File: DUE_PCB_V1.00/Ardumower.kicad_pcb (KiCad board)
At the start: 2 copper layers, 169.9 x 97 mm, 81 parts, among them J1 9V IN, J10 Sonar_R, J11 Sonar_C, J12 Sonar_L, J13 P_Right, J14 Buzzer, J15 Button, J16 US1, J17 US2, J18 US3, J19 P_Left, J2 I2C0_1, J20 Remote, J21 PCB_2, J22 Ser0, J23 Ser1, J24 Ser2, J25 5V IN, J26 Cutter1, J27 MotorR, J28 MotorL, J29 3.3V IN, J3 I2C0_2, J30 I2C1_2, J31 Ser3, J32 24V In, J33 ReserveD8, J34 ReserveD9, J35 ReserveD49, J36 ReserveA10, J37 RPM_Mow, J38 ODO_Left, J39 ODO_Right, J4 I2C1_1, J5 Bumper, J6 Drop_Left, J7 Drop_Right, J8 Tilt, J9 Rain, U1 MC33926, U2 MC33926

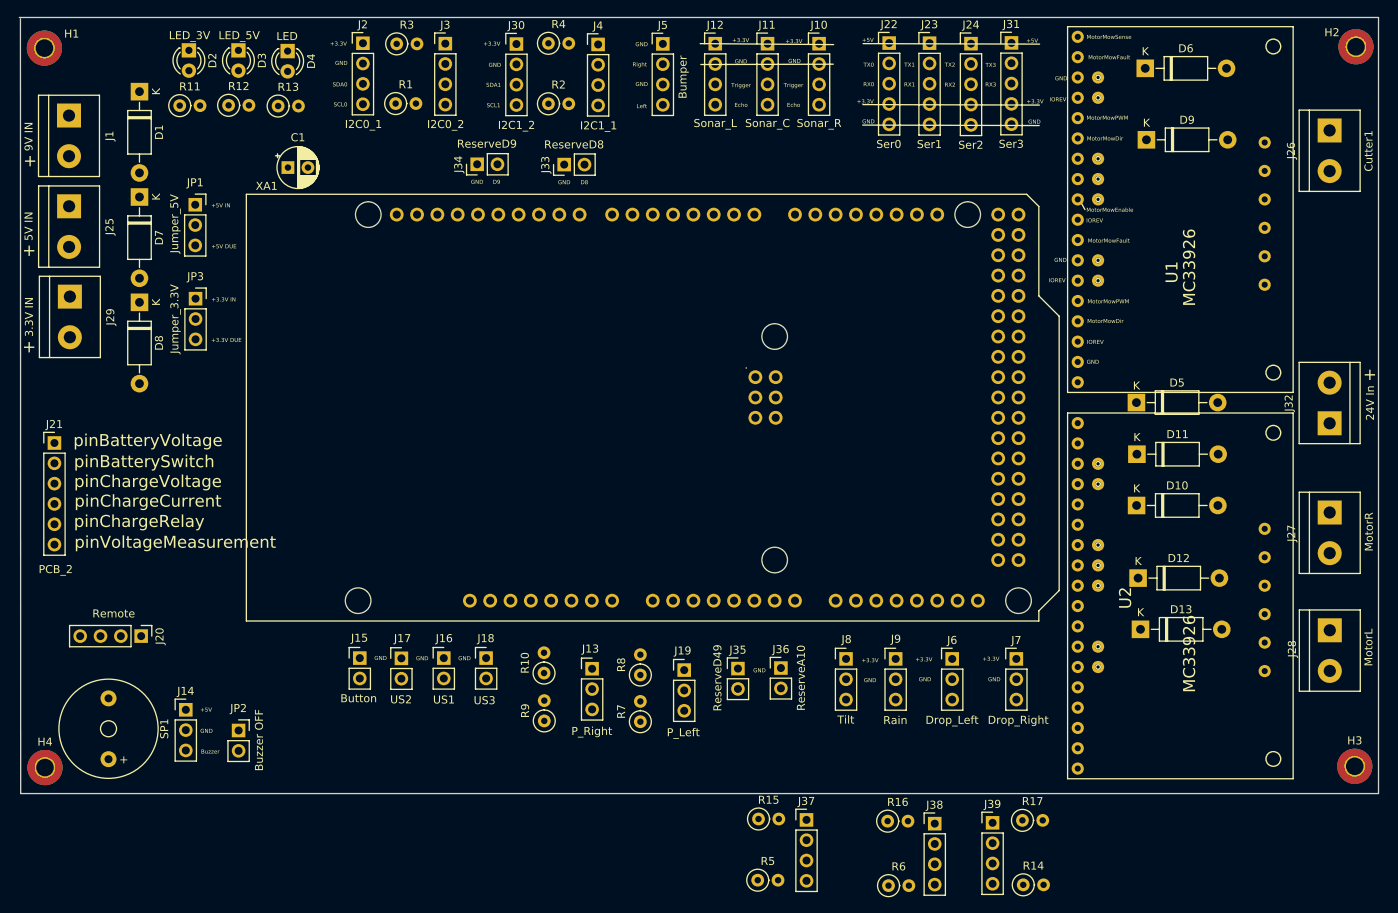
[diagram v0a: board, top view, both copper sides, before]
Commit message: Sorting Connectors on PCB
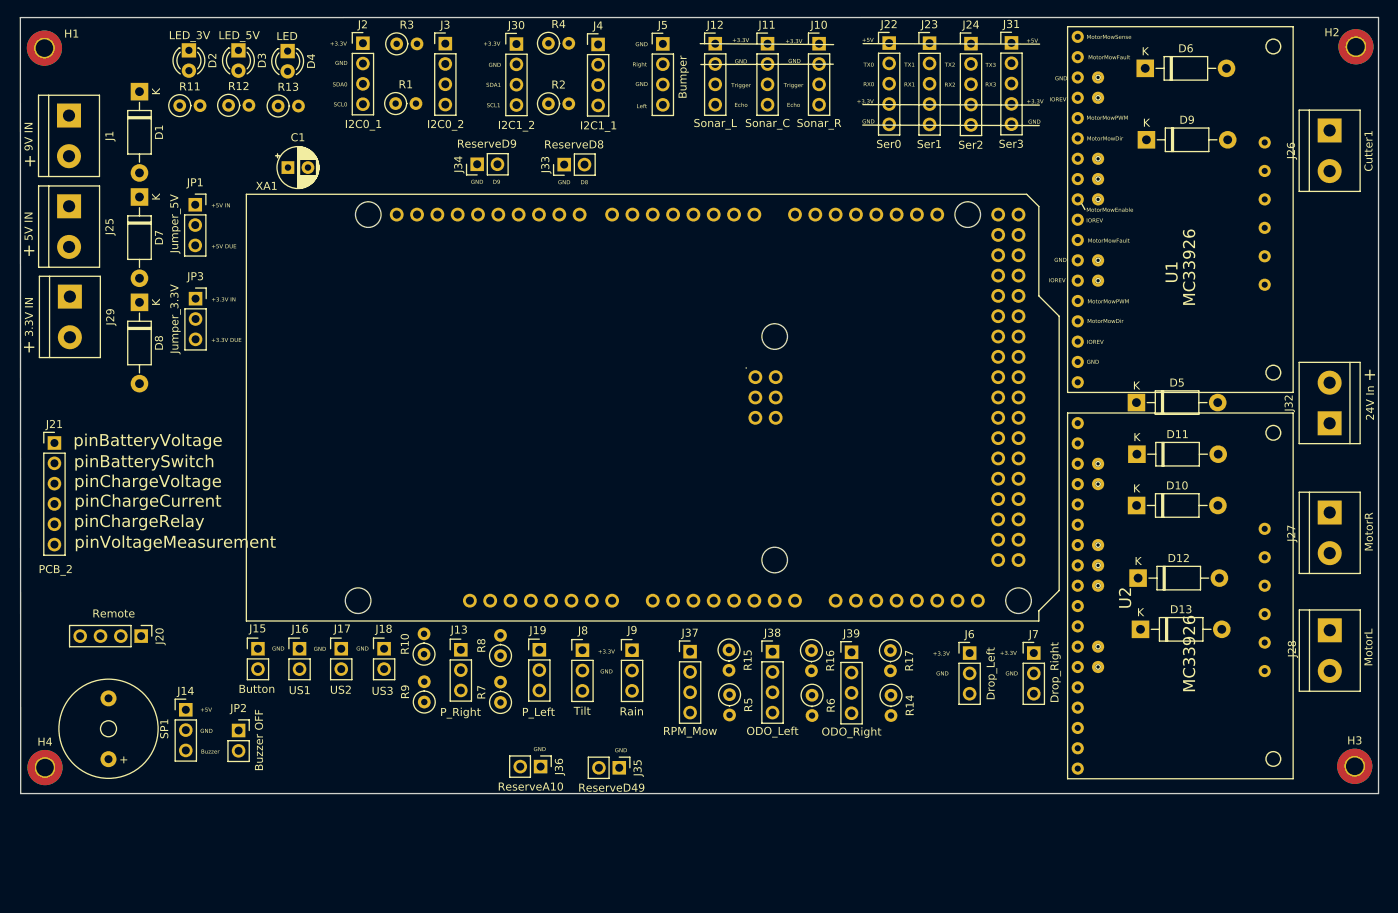
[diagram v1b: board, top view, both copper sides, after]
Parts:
- moved J9 33.0 mm to (115.3, 113.7)
- moved J8 33.0 mm to (109.1, 113.7)
- moved J36 32.5 mm to (103.8, 128.2), turned to 270 degrees
- moved J38 29.6 mm to (132.8, 113.9)
- moved R14 28.9 mm to (147.6, 119.3), turned to 270 degrees
- moved J39 27.7 mm to (142.7, 114.0)
- moved R17 26.9 mm to (147.6, 113.7), turned to 270 degrees
- moved R6 25.6 mm to (137.8, 119.3), turned to 270 degrees
- moved J37 25.6 mm to (122.5, 113.9)
- moved R5 23.5 mm to (127.5, 119.3), turned to 270 degrees
- moved R16 23.4 mm to (137.7, 113.7), turned to 270 degrees
- moved R15 21.4 mm to (127.4, 113.7), turned to 270 degrees
- moved J35 19.3 mm to (113.7, 128.4), turned to 270 degrees
- moved J19 18.3 mm to (103.7, 113.7)
- moved J16 18.1 mm to (73.7, 113.5)
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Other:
- board size 169.9 x 97 mm -> 169.8 x 97 mm

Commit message: Change direction from i2c Pins
Change direction from i2c Pins to pass with other pins direction
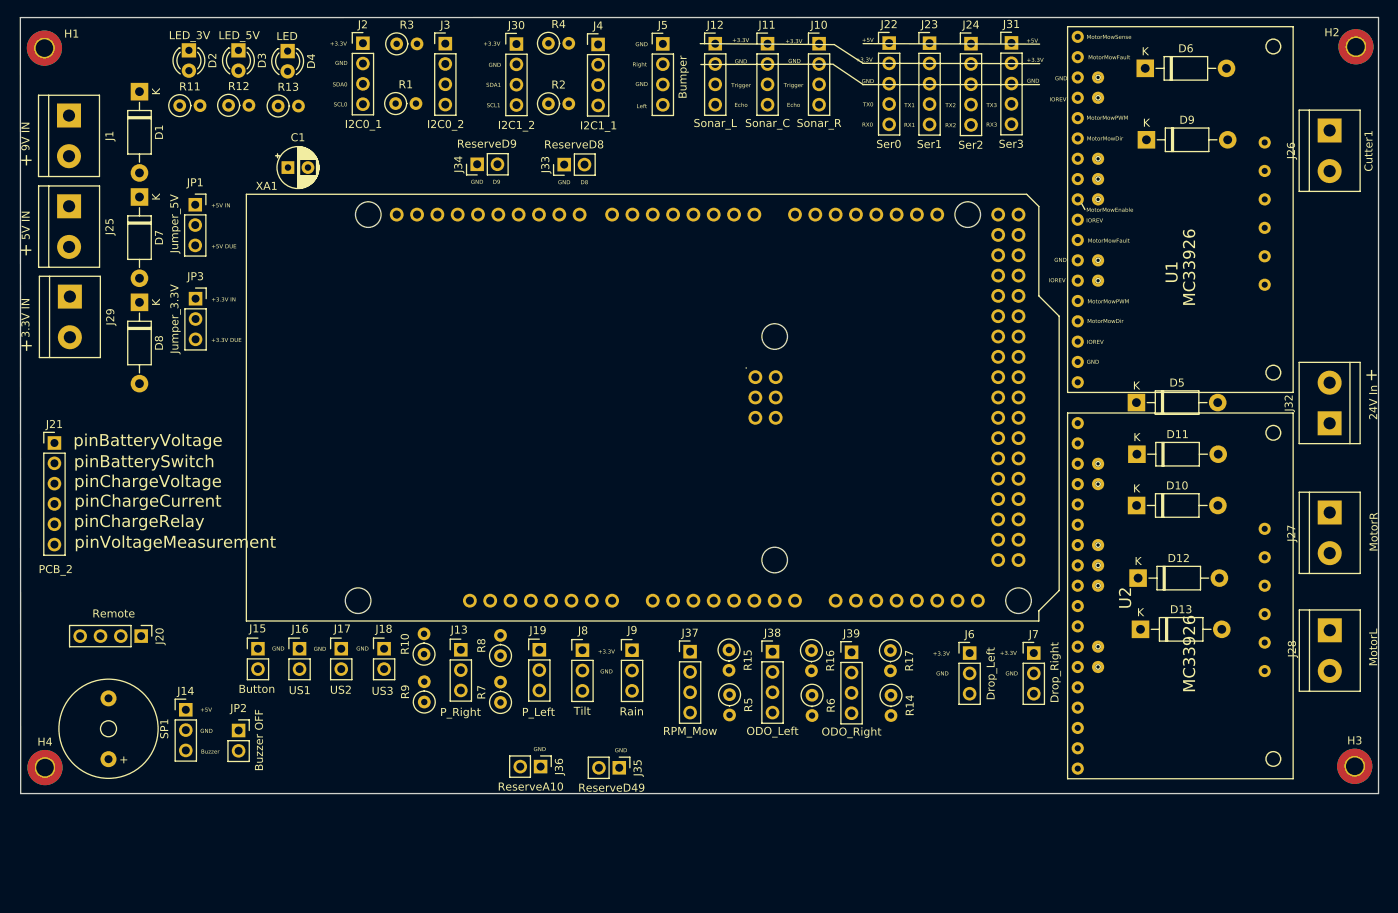
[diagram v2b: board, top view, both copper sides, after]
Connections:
- J22 pad 2: TX0 -> +3V3
- J22 pad 3: RX0 -> GND
- J22 pad 4: +3V3 -> TX0
- J22 pad 5: GND -> RX0
- J23 pad 2: TX1 -> +3V3
- J23 pad 3: RX1 -> GND
- J23 pad 4: +3V3 -> TX1
- J23 pad 5: GND -> RX1
- J24 pad 2: TX2 -> +3V3
- J24 pad 3: RX2 -> GND
- J24 pad 4: +3V3 -> TX2
- J24 pad 5: GND -> RX2
- J31 pad 2: TX3 -> +3V3
- J31 pad 3: RX3 -> GND
- J31 pad 4: +3V3 -> TX3
- J31 pad 5: GND -> RX3

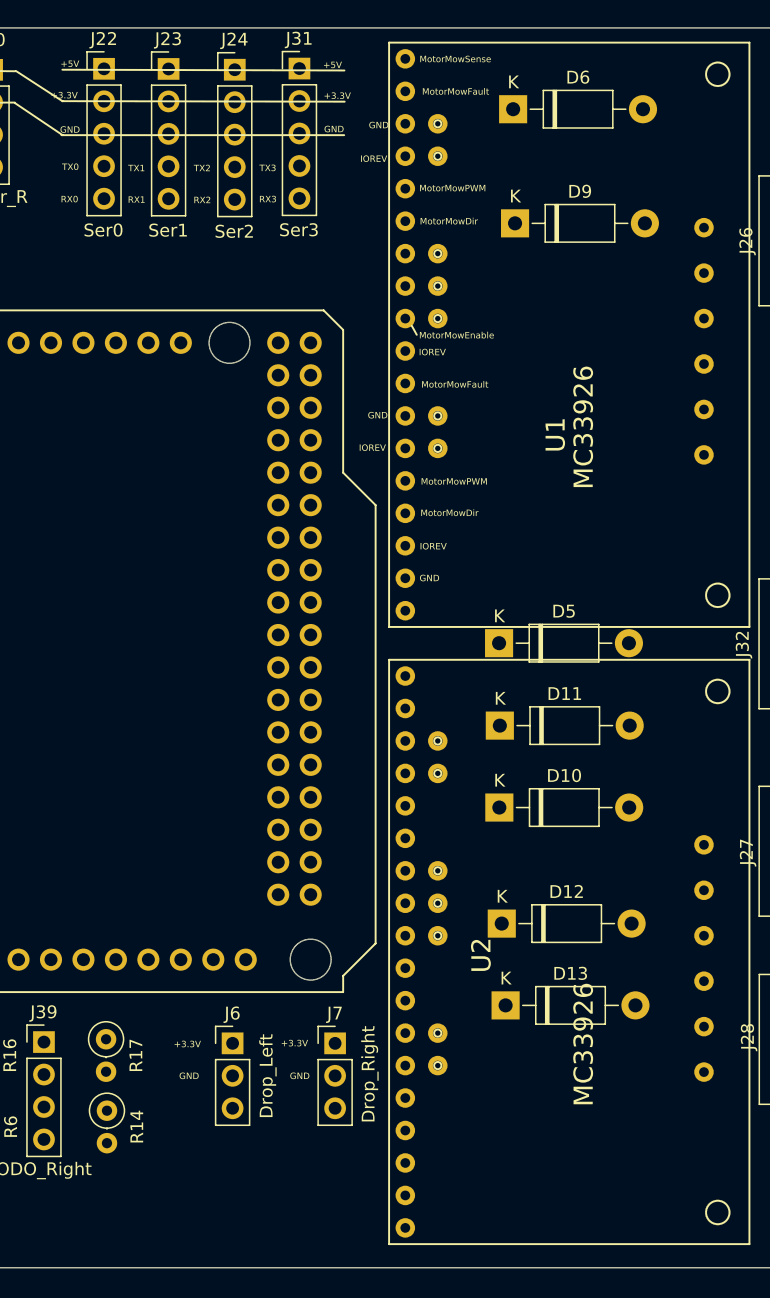
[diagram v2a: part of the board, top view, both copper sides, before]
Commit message: Add Motor Connectors
Add Default Motor Connectors and reorder Ser0-Ser3
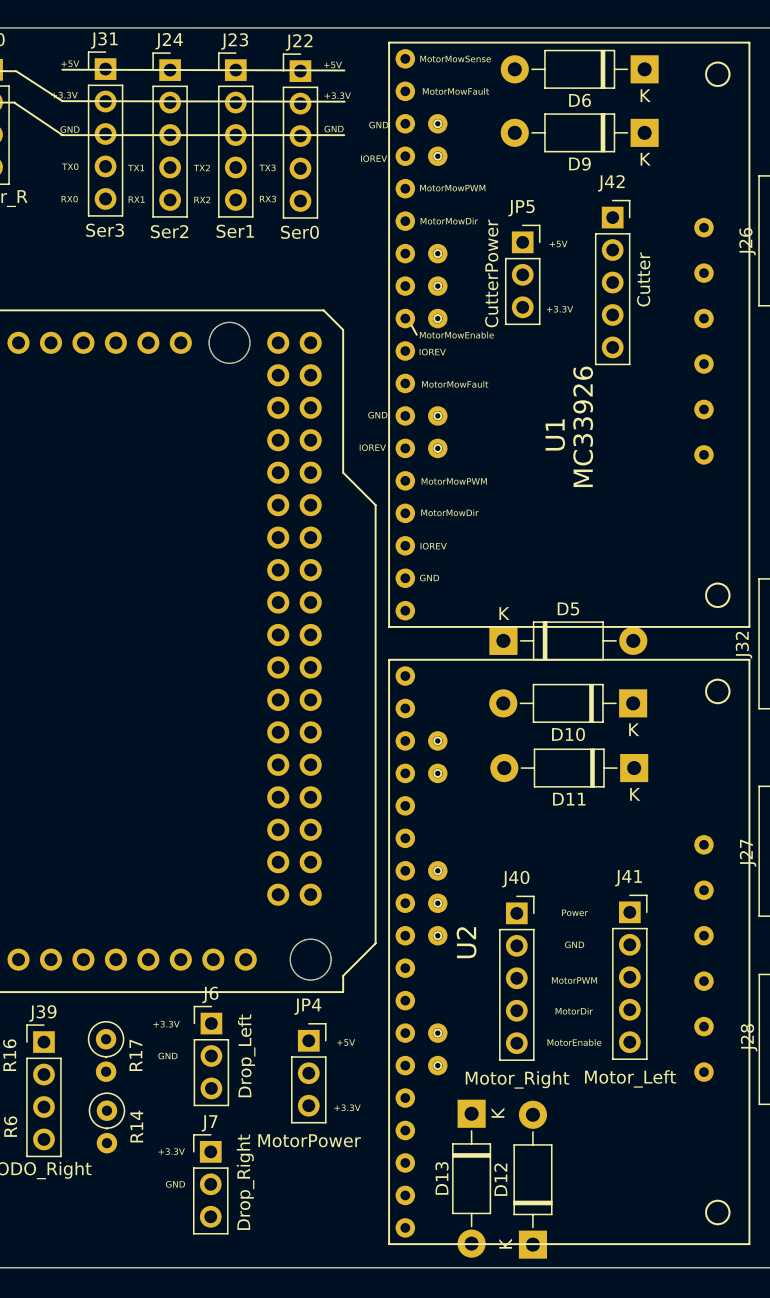
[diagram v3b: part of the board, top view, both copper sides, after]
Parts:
- added J40: Motor_Right, Connector_PinSocket_2.54mm:PinSocket_1x05_P2.54mm_Vertical, F.Cu at (179.7, 103.9)
- added J41: Motor_Left, Connector_PinSocket_2.54mm:PinSocket_1x05_P2.54mm_Vertical, F.Cu at (188.5, 103.8)
- added J42: Cutter, Connector_PinSocket_2.54mm:PinSocket_1x05_P2.54mm_Vertical, F.Cu at (187.2, 49.5)
- added JP4: MotorPower, Connector_PinSocket_2.54mm:PinSocket_1x03_P2.54mm_Vertical, F.Cu at (163.4, 113.9)
- added JP5: CutterPower, Connector_PinSocket_2.54mm:PinSocket_1x03_P2.54mm_Vertical, F.Cu at (180.2, 51.4)
- D5: value 1N5819 -> 1N4728A
- moved D12 25.2 mm to (181.0, 129.8), turned to 90 degrees
- moved J22 15.4 mm to (162.8, 38.0)
- moved J31 15.2 mm to (147.5, 37.8)
- moved D10 13.3 mm to (188.8, 87.5), turned to 180 degrees
- moved J7 12.9 mm to (155.8, 122.5)
- moved D9 12.4 mm to (189.7, 42.8), turned to 180 degrees
- moved D11 11.0 mm to (188.9, 92.5), turned to 180 degrees
- moved D6 10.8 mm to (189.7, 37.9), turned to 180 degrees
- moved D13 8.89 mm to (176.2, 119.6), turned to 270 degrees
- moved J23 5.26 mm to (157.7, 37.9)
- moved J24 5.06 mm to (152.6, 37.9)
- moved J6 2.27 mm to (155.8, 112.5)
- moved D5 0.38 mm to (178.7, 82.6)
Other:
- board text added: "MotorDir"
- board text added: "MotorEnable"
- board text added: "MotorPWM"
- board text added: "Power"
